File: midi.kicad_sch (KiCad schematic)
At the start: 20 parts, among them CN1 MIDI Out 1, CN2 MIDI In 1, CN3 MIDI Out 2, CN4 MIDI In 2, J4 UART46, J5 UART5, U6 6N137S-TA1, U7 6N137S-TA1

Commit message: Finished checking all parts against LCSC IDs. Found remaining errors. Added manufacturer part numbers to all parts.
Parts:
- C20, C44: Manu Part (none) -> CL05B104KB54PNC; Manufacturer (none) -> Samsung Electro-Mechanics
- R13, R14, R26, R27: JLC Basic Part Extended -> Extended - Basic is C23182 but 0603
- R15, R28: JLC Basic Part (none) -> Basic; Manu Part (none) -> 0402WGF2200TCE; Manufacturer (none) -> UNI-ROYAL(Uniroyal Elec)
- R16, R29: JLC Basic Part (none) -> Basic; Manu Part (none) -> 0402WGF4700TCE; Manufacturer (none) -> UNI-ROYAL(Uniroyal Elec)
- U6, U7: DPFNOTES (none) -> 15Mbit/s 4.5V~5.5V 10kV/us DC SOP-8-2.54mm Logic Output Opt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; JLC Basic Part (none) -> Extended; Manu Part (none) -> 6N137S-TA1-L; Manufacturer (none) -> Lite-On
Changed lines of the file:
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@@
 			)
 		)
-		(property "Manu Part" ""
+		(property "Manu Part" "6N137S-TA1-L"
 			(at 78.74 104.14 0)
 			(effects
@@
 			)
 		)
-		(property "Manufacturer" ""
+		(property "Manufacturer" "Lite-On"
 			(at 78.74 104.14 0)
 			(effects
@@
 		)
 		(property "FIXME" ""
+			(at 78.74 104.14 0)
+			(effects
+				(font
+					(size 1.27 1.27)
+				)
+				(hide yes)
+			)
+		)
+		(property "DPFNOTES" "15Mbit/s 4.5V~5.5V 10kV/us DC SOP-8-2.54mm Logic Output Optoisolators ROHS"
+			(at 78.74 104.14 0)
+			(effects
+				(font
+					(size 1.27 1.27)
+				)
+				(hide yes)
+			)
+		)
+		(property "JLC Basic Part" "Extended"
 			(at 78.74 104.14 0)
 			(effects
@@
 			)
 		)
-		(property "Manu Part" ""
+		(property "Manu Part" "0402WGF4700TCE"
 			(at 99.06 49.53 0)
 			(effects
@@
 			)
 		)
-		(property "Manufacturer" ""
+		(property "Manufacturer" "UNI-ROYAL(Uniroyal Elec)"
 			(at 99.06 49.53 0)
 			(effects
@@
 		)
 		(property "FIXME" ""
+			(at 99.06 49.53 0)
+			(effects
+				(font
+					(size 1.27 1.27)
+				)
+				(hide yes)
+			)
+		)
+		(property "JLC Basic Part" "Basic"
 			(at 99.06 49.53 0)
 			(effects
@@
 			)
 		)
-		(property "Manu Part" ""
+		(property "Manu Part" "6N137S-TA1-L"
 			(at 78.74 52.07 0)
 			(effects
@@
 			)
 		)
-		(property "Manufacturer" ""
+		(property "Manufacturer" "Lite-On"
 			(at 78.74 52.07 0)
 			(effects
@@
 		)
 		(property "FIXME" ""
+			(at 78.74 52.07 0)
+			(effects
+				(font
+					(size 1.27 1.27)
+				)
+				(hide yes)
+			)
+		)
+		(property "DPFNOTES" "15Mbit/s 4.5V~5.5V 10kV/us DC SOP-8-2.54mm Logic Output Optoisolators ROHS"
+			(at 78.74 52.07 0)
+			(effects
+				(font
+					(size 1.27 1.27)
+				)
+				(hide yes)
+			)
+		)
+		(property "JLC Basic Part" "Extended"
 			(at 78.74 52.07 0)
 			(effects
@@
 			)
 		)
-		(property "JLC Basic Part" "Extended"
+		(property "JLC Basic Part" "Extended - Basic is C23182 but 0603"
 			(at 46.99 86.36 0)
 			(effects
@@
 			)
 		)
-		(property "JLC Basic Part" "Extended"
+		(property "JLC Basic Part" "Extended - Basic is C23182 but 0603"
 			(at 46.99 31.75 0)
 			(effects
@@
 			)
 		)
-		(property "Manu Part" ""
+		(property "Manu Part" "CL05B104KB54PNC"
 			(at 123.19 102.87 0)
 			(effects
@@
 			)
 		)
-		(property "Manufacturer" ""
+		(property "Manufacturer" "Samsung Electro-Mechanics"
 			(at 123.19 102.87 0)
 			(effects
@@
 			)
 		)
-		(property "Manu Part" ""
+		(property "Manu Part" "0402WGF4700TCE"
 			(at 99.06 101.6 0)
 			(effects
@@
 			)
 		)
-		(property "Manufacturer" ""
+		(property "Manufacturer" "UNI-ROYAL(Uniroyal Elec)"
 			(at 99.06 101.6 0)
 			(effects
@@
 		)
 		(property "FIXME" ""
+			(at 99.06 101.6 0)
+			(effects
+				(font
+					(size 1.27 1.27)
+				)
+				(hide yes)
+			)
+		)
+		(property "JLC Basic Part" "Basic"
 			(at 99.06 101.6 0)
 			(effects
@@
 			)
 		)
-		(property "Manu Part" ""
+		(property "Manu Part" "0402WGF2200TCE"
 			(at 49.53 48.26 0)
 			(effects
@@
 			)
 		)
-		(property "Manufacturer" ""
+		(property "Manufacturer" "UNI-ROYAL(Uniroyal Elec)"
 			(at 49.53 48.26 0)
 			(effects
@@
 		)
 		(property "FIXME" ""
+			(at 49.53 48.26 0)
+			(effects
+				(font
+					(size 1.27 1.27)
+				)
+				(hide yes)
+			)
+		)
+		(property "JLC Basic Part" "Basic"
 			(at 49.53 48.26 0)
 			(effects
@@
 			)
 		)
-		(property "JLC Basic Part" "Extended"
+		(property "JLC Basic Part" "Extended - Basic is C23182 but 0603"
 			(at 46.99 83.82 0)
 			(effects
@@
 			)
 		)
-		(property "Manu Part" ""
+		(property "Manu Part" "CL05B104KB54PNC"
 			(at 123.19 50.8 0)
 			(effects
@@
 			)
 		)
-		(property "Manufacturer" ""
+		(property "Manufacturer" "Samsung Electro-Mechanics"
 			(at 123.19 50.8 0)
 			(effects
@@
 			)
 		)
-		(property "JLC Basic Part" "Extended"
+		(property "JLC Basic Part" "Extended - Basic is C23182 but 0603"
 			(at 46.99 34.29 0)
 			(effects
@@
 			)
 		)
-		(property "Manu Part" ""
+		(property "Manu Part" "0402WGF2200TCE"
 			(at 49.53 100.33 0)
 			(effects
@@
 			)
 		)
-		(property "Manufacturer" ""
+		(property "Manufacturer" "UNI-ROYAL(Uniroyal Elec)"
 			(at 49.53 100.33 0)
 			(effects
@@
 			(at 49.53 100.33 0)
 			(effects
+				(font
+					(size 1.27 1.27)
+				)
+				(hide yes)
+			)
+		)
+		(property "JLC Basic Part" "Basic"
+			(at 49.53 100.33 0)
+			(effects

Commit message: Received EVT #1 boards. Updating based on errors found so far. Added revision page. First error was misunderstanding the TRS connector pinout/schematic.
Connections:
- net GND: now also CN1.1, CN2.1; no longer CN1.2, CN2.2
- net MI1-SNK: now also CN2.2; no longer CN2.1
- net MO1-SNK: now also CN1.2; no longer CN1.1
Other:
- note added: "1 = Sleeve 3 = Ring 2 = Tip"
- note added: "Image credit: https://www.sameskydevices.com/blog/understanding-audio-jack-switches-and-schematics"
- note added: "TODO: Fix this schematic!"
- note removed: "Ring = 3"
- note removed: "Sleeve = 2"
- note removed: "Tip = 1"
- moved on the sheet: R13, R14

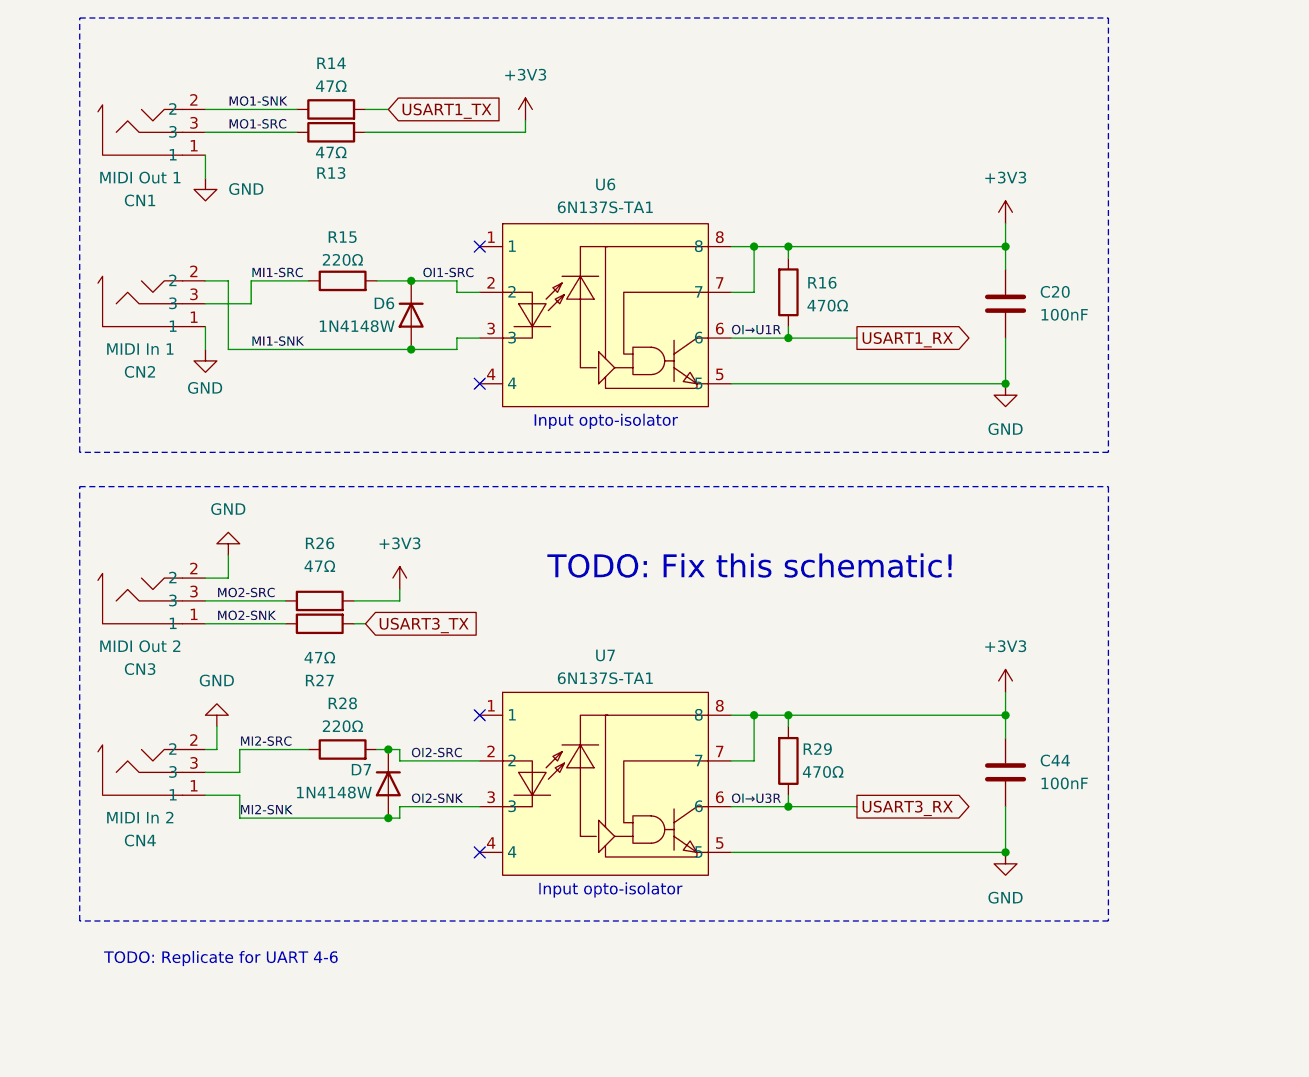
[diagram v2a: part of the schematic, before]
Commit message: 1. Fixed mis-wired 3.5mm jacks everywhere. 2. Use smaller opto-isolator and diode with updated circuit for one MIDI.
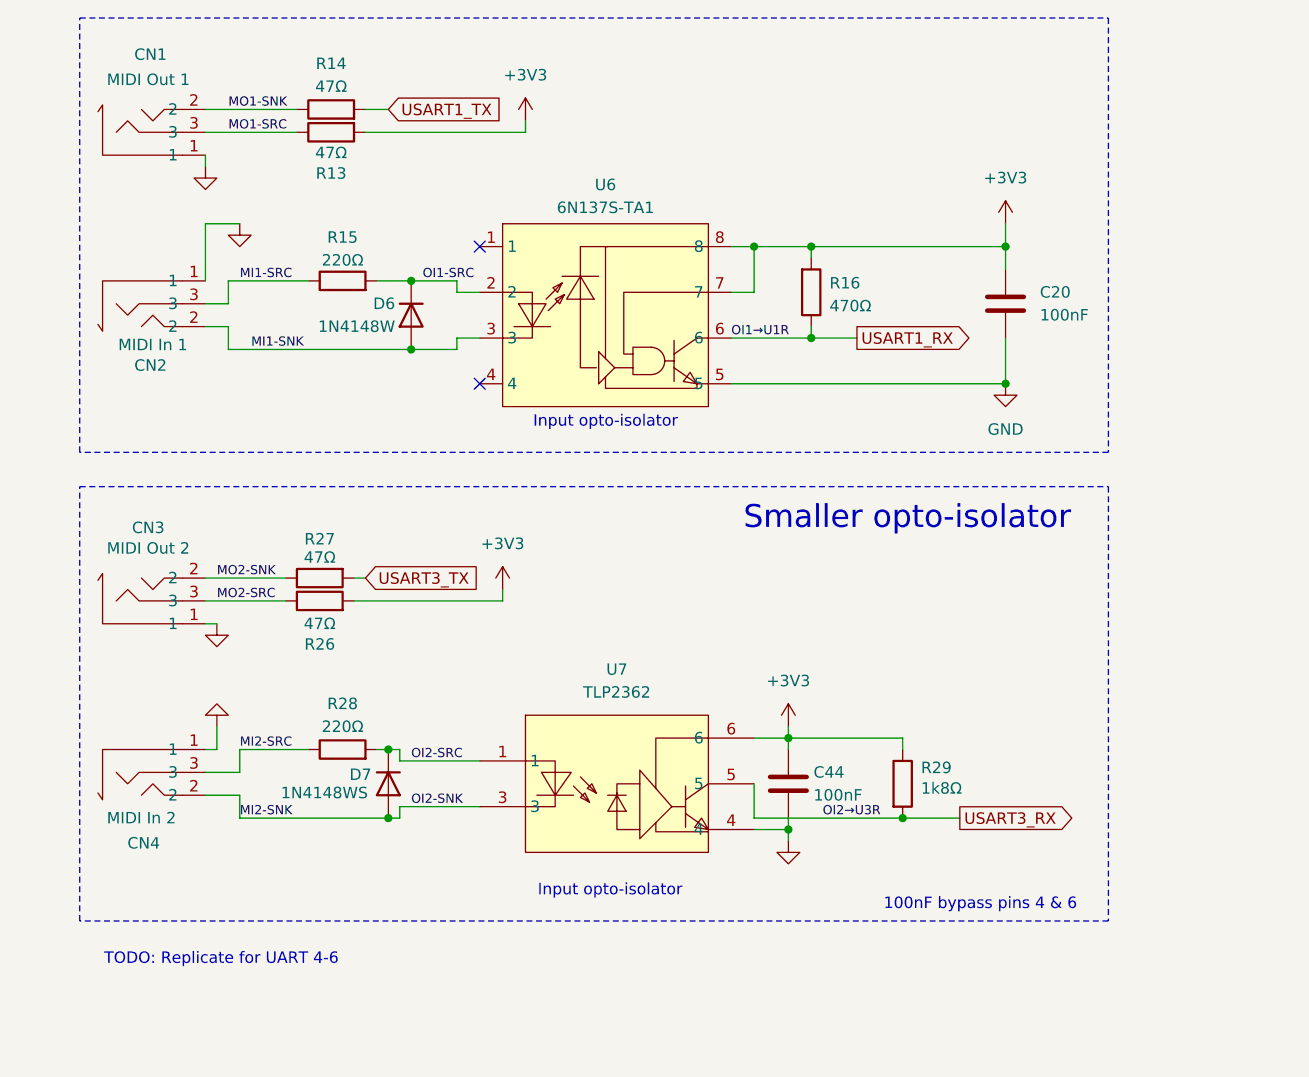
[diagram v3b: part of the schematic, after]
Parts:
- removed D7: 1N4148W, Diode_SMD:D_SOD-123, symbol Diode:1N4148W
- removed U7: 6N137S-TA1, easyeda2kicad:SOP-8_L9.8-W6.6-P2.54-LS10.3-BL, symbol easyeda2kicad:6N137S-TA1
- added D7: 1N4148WS, Diode_SMD:D_SOD-323, symbol Diode:1N4148WS
- added U7: TLP2362, easyeda2kicad:OPTO-SMD-5_L3.7-W4.6-P1.27-LS7.0-BR, symbol easyeda2kicad:TLP2362(TPL,E(T
- R29: value 470Ω -> 1k8Ω; DPFNOTES 62.5mW Thick Film Resistors 50V ±100ppm/℃ ±1% 470Ω 0402 Chi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 -> 62.5mW Thick Film Resistors 50V ±100ppm/℃ ±1% 1.8kΩ 0402 Ch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; JLC Basic Part Basic -> Extended - Basic is C4177 but is 0603; LCSC C25117 -> C25871; Manu Part 0402WGF4700TCE -> 0402WGF1801TCE
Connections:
- net +3V3: now also R29.1, U7.6; no longer R29.2
- net GND: now also CN3.1, CN4.1, U7.4; no longer CN3.2, CN4.2
- net MI2-SNK: now also CN4.2, D7.2 (A), U7.3; no longer CN4.1
- net MO2-SNK: now also CN3.2; no longer CN3.1
- net OI2-SRC: now also D7.1 (K), U7.1
- net USART3_RX: now also R29.2, U7.5; no longer R29.1
- no-connect marks 4 -> 2
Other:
- note added: "100nF bypass pins 4 & 6"
- note added: "Smaller opto-isolator"
- note removed: "TODO: Fix this schematic!"
- moved on the sheet: C44, R16, R27

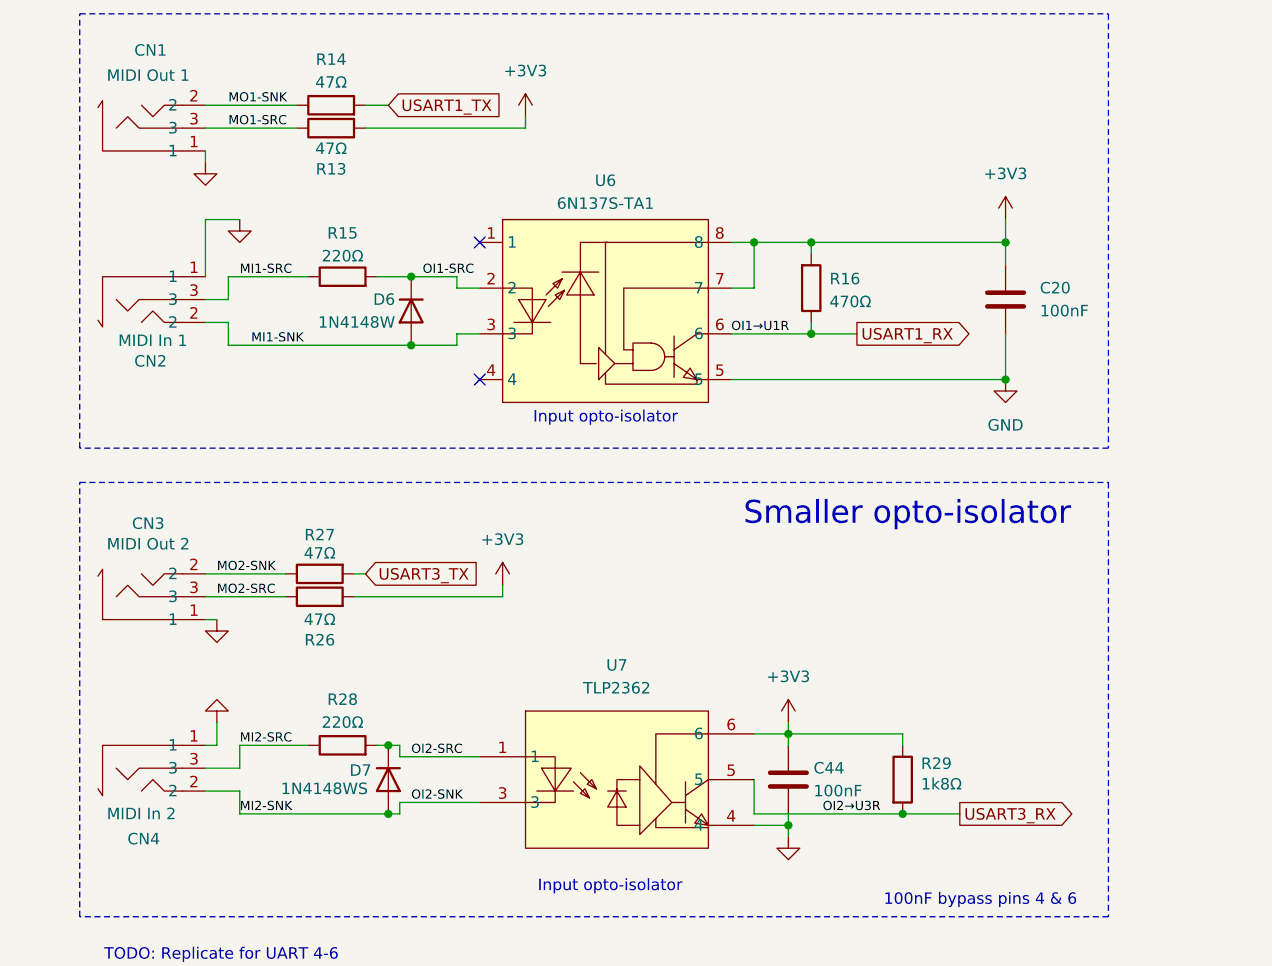
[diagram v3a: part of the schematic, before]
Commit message: Move MIDI1 to the new opto-isolator circuit. Update silkscreen with EVT#2.
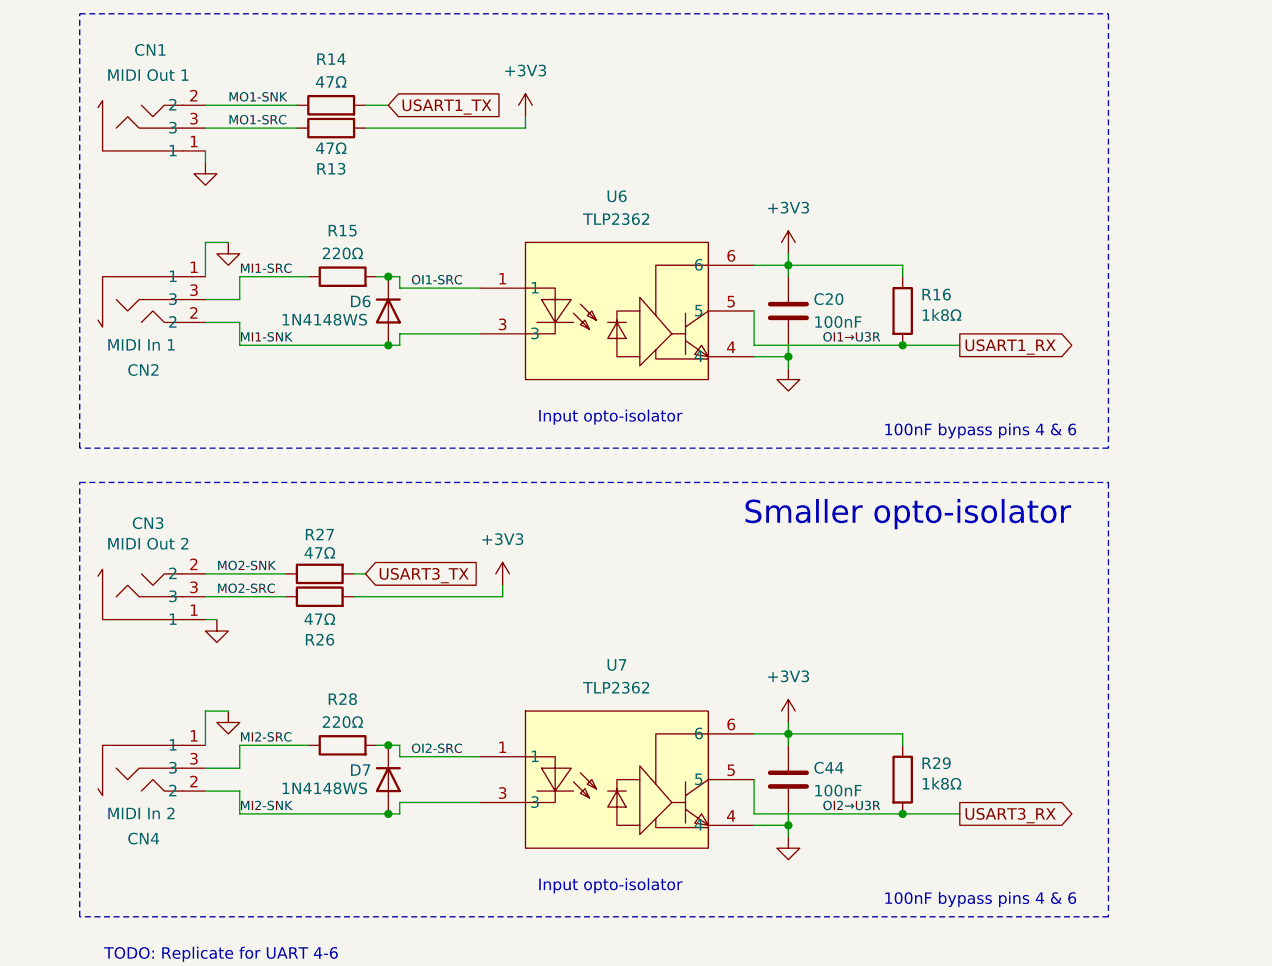
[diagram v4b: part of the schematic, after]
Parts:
- removed D6: 1N4148W, Diode_SMD:D_SOD-123, symbol Diode:1N4148W
- removed U6: 6N137S-TA1, easyeda2kicad:SOP-8_L9.8-W6.6-P2.54-LS10.3-BL, symbol easyeda2kicad:6N137S-TA1
- added D6: 1N4148WS, Diode_SMD:D_SOD-323, symbol Diode:1N4148WS
- added U6: TLP2362, easyeda2kicad:OPTO-SMD-5_L3.7-W4.6-P1.27-LS7.0-BR, symbol easyeda2kicad:TLP2362(TPL,E(T
- R16: value 470Ω -> 1k8Ω; DPFNOTES 62.5mW Thick Film Resistors 50V ±100ppm/℃ ±1% 470Ω 0402 Chi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 -> 62.5mW Thick Film Resistors 50V ±100ppm/℃ ±1% 1.8kΩ 0402 Ch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; JLC Basic Part Basic -> Extended - Basic is C4177 but is 0603; LCSC C25117 -> C25871; Manu Part 0402WGF4700TCE -> 0402WGF1801TCE
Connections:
- net +3V3: now also R16.1, U6.6; no longer R16.2
- net GND: now also U6.4
- net MI1-SNK: now also D6.2 (A), U6.3
- net OI1-SRC: now also D6.1 (K), U6.1
- net USART1_RX: now also R16.2, U6.5; no longer R16.1
- no-connect marks 2 -> 0

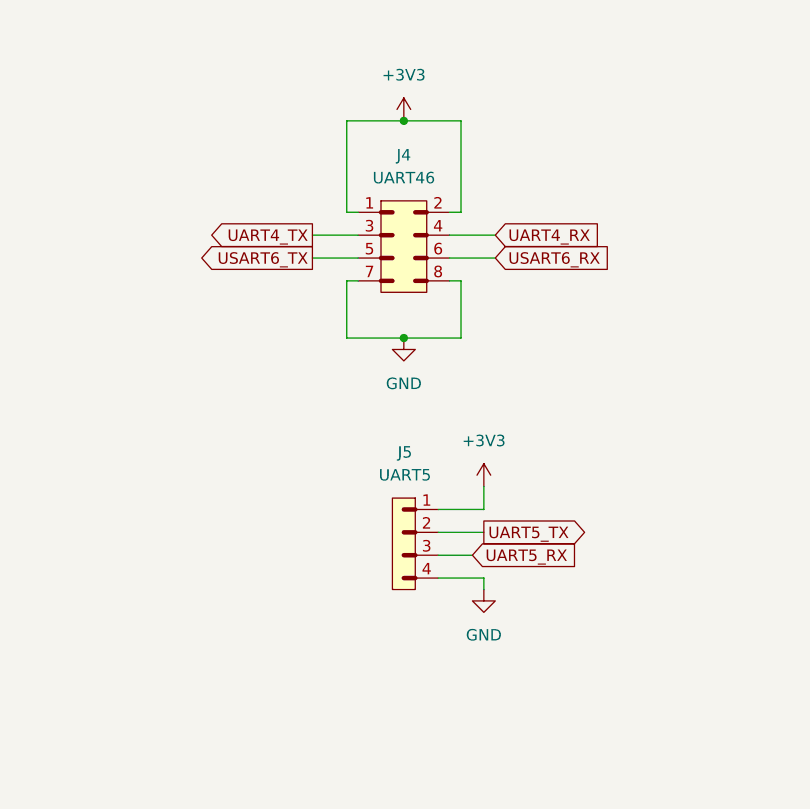
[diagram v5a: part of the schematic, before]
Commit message: Consolidate UART5 with 4 & 6 on a single header
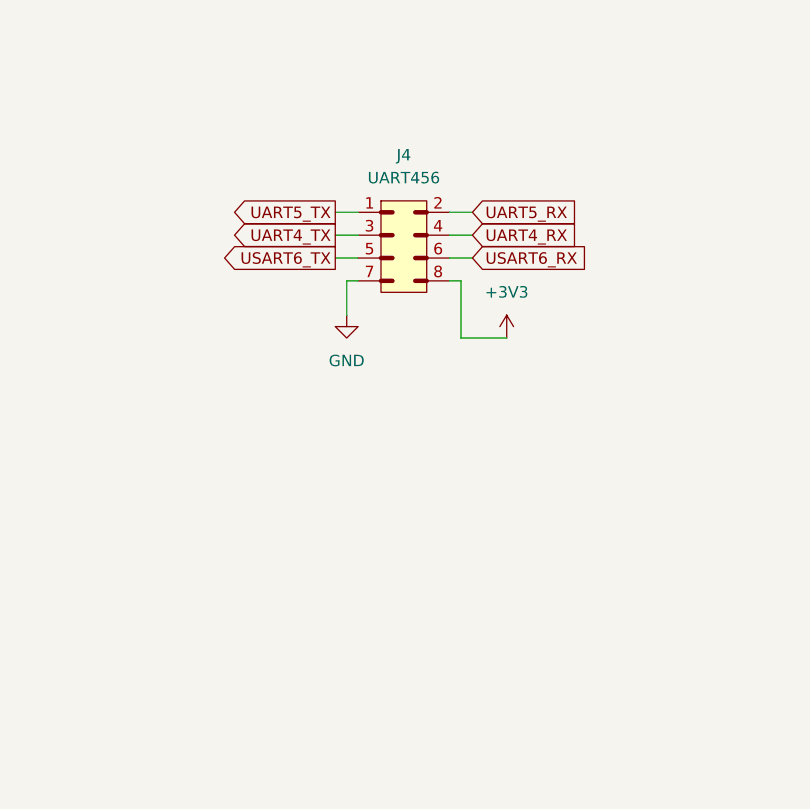
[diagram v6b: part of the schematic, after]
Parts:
- removed J5: UART5, Connector_PinHeader_2.54mm:PinHeader_1x04_P2.54mm_Vertical, symbol PCM_SL_Pin_Headers:PINHD_1x4_Male
- J4: value UART46 -> UART456
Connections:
- net +3V3: now also J4.8; no longer J4.1, J4.2
- net GND: no longer J4.8
- net UART5_RX: now also J4.2
- net UART5_TX: now also J4.1
